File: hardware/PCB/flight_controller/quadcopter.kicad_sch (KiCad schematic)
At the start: 31 parts

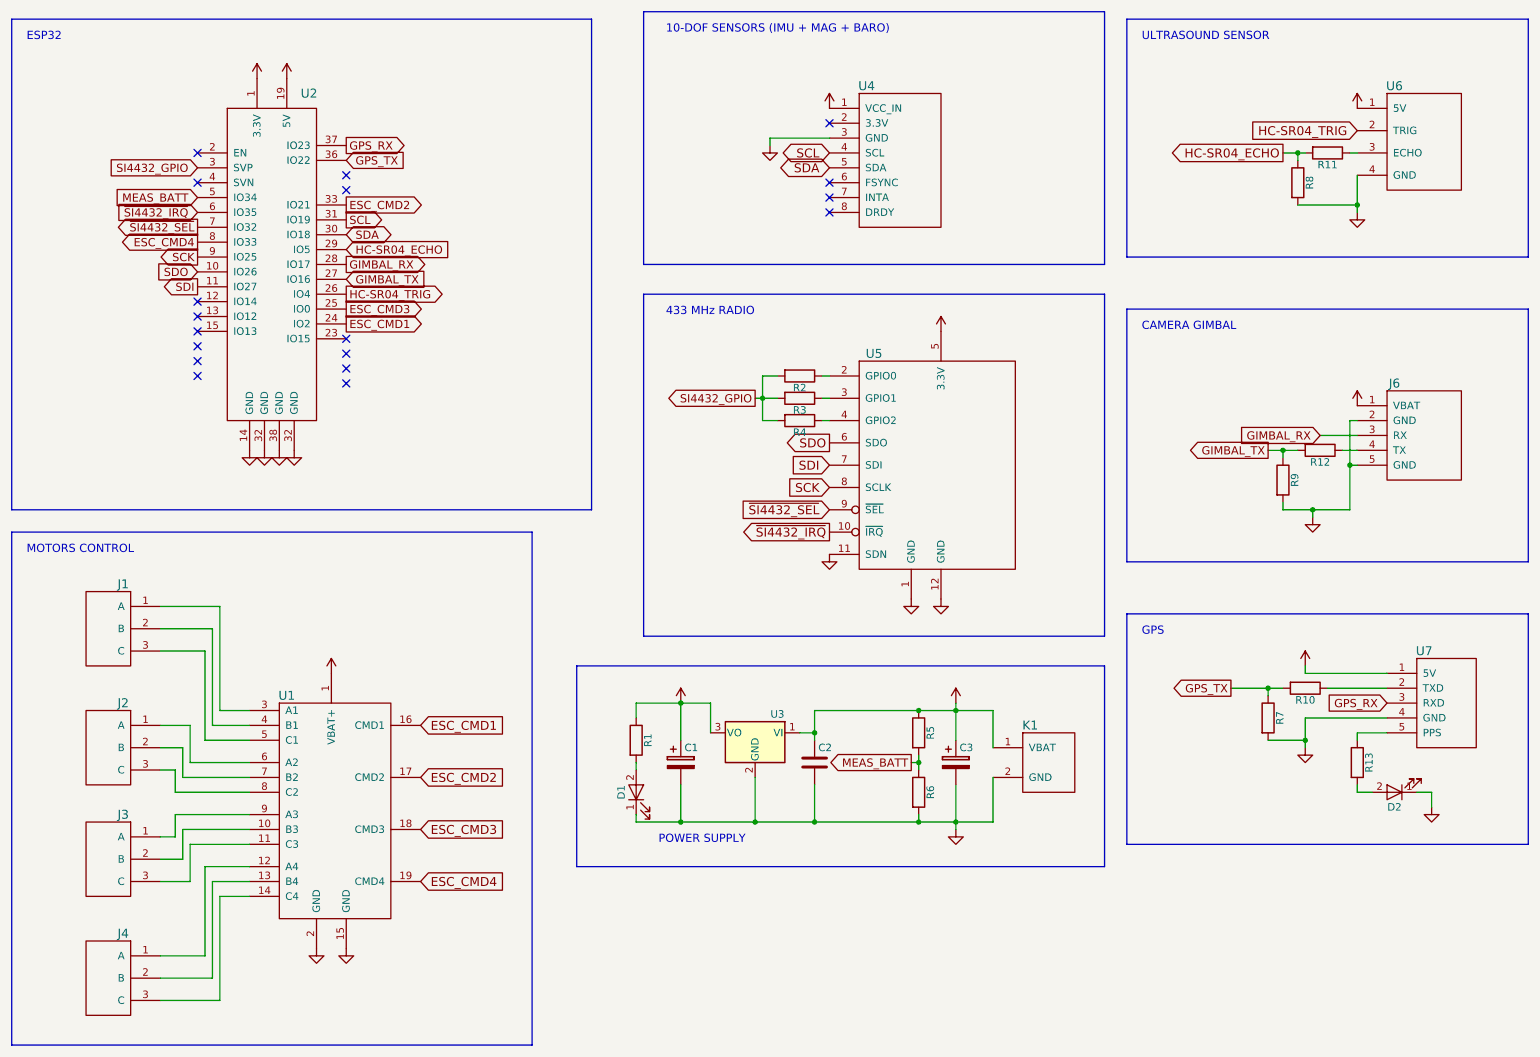
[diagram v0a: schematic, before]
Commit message: Move flight_controller PCB
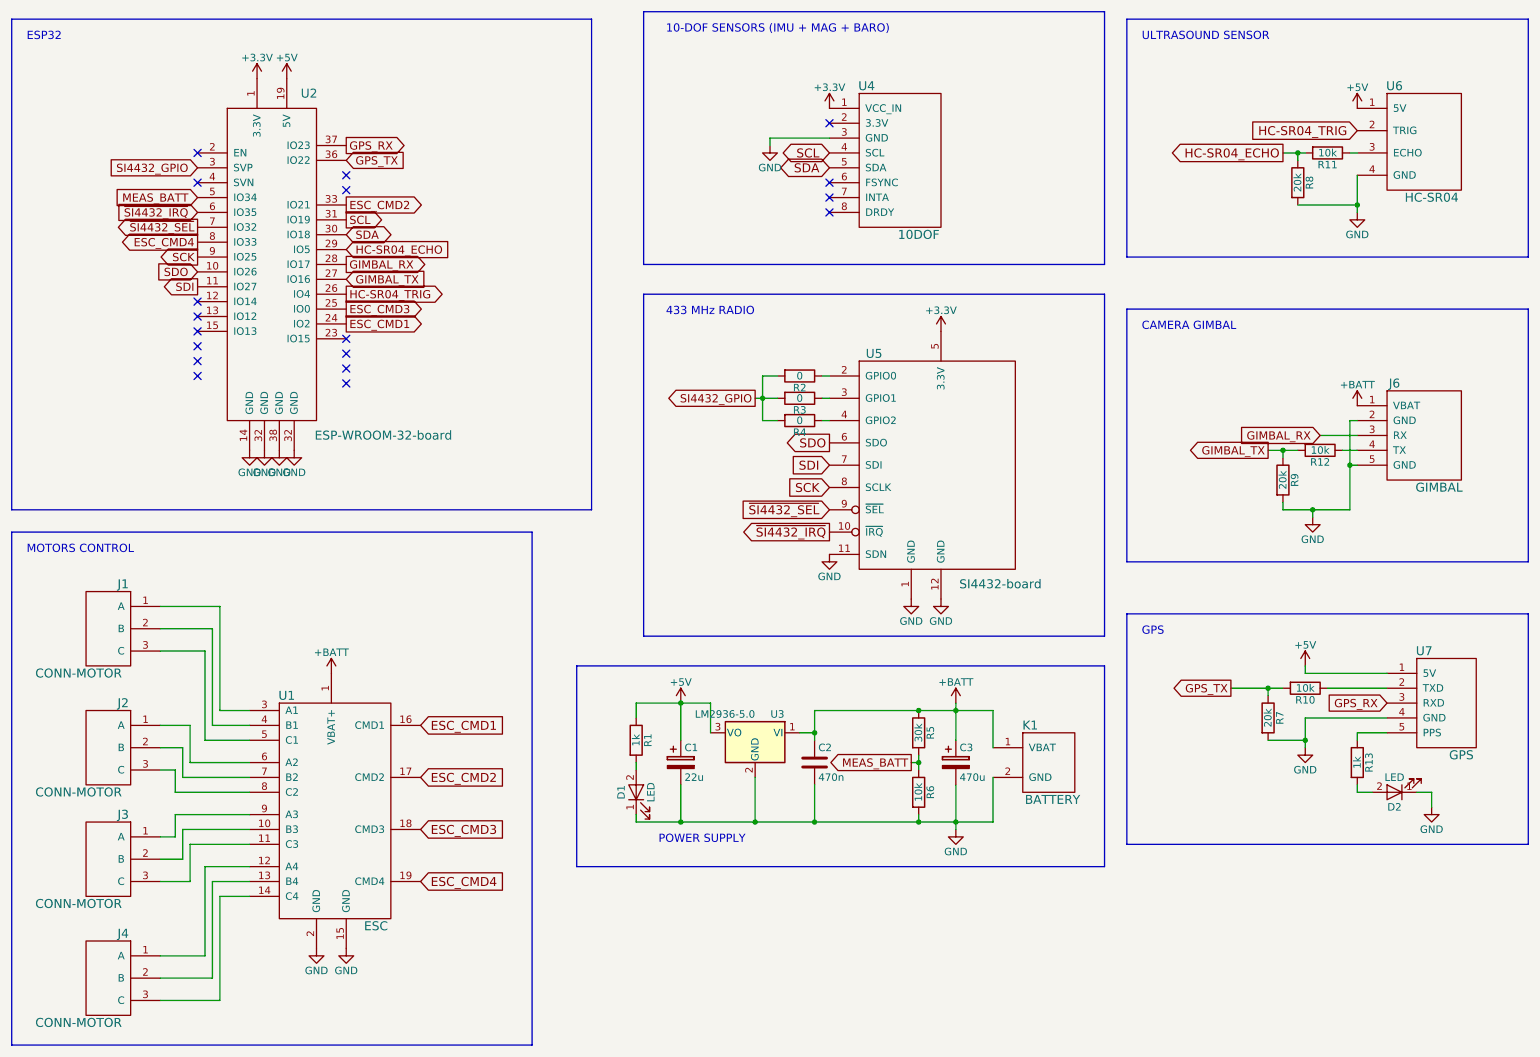
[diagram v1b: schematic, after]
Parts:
- C1: value (none) -> 22u; footprint (none) -> Capacitor_THT:CP_Radial_D5.0mm_P2.50mm
- C2: value (none) -> 470n; footprint (none) -> Capacitor_SMD:C_1206_3216Metric_Pad1.42x1.75mm_HandSolder
- C3: value (none) -> 470u; footprint (none) -> Capacitor_THT:CP_Radial_D10.0mm_P5.00mm
- D1, D2: value (none) -> LED; footprint (none) -> LED_SMD:LED_1206_3216Metric_Pad1.42x1.75mm_HandSolder
- J1, J2, J3, J4: value (none) -> CONN-MOTOR; footprint (none) -> quadcopter:motor-connector
- J6: value (none) -> GIMBAL; footprint (none) -> quadcopter:GIMBAL
- K1: value (none) -> BATTERY; footprint (none) -> quadcopter:battery-connector
- R1, R13: value (none) -> 1k; footprint (none) -> Resistor_SMD:R_1206_3216Metric_Pad1.42x1.75mm_HandSolder
- R10, R11, R12, R6: value (none) -> 10k; footprint (none) -> Resistor_SMD:R_1206_3216Metric_Pad1.42x1.75mm_HandSolder
- R2, R3, R4: value (none) -> 0; footprint (none) -> Resistor_SMD:R_1206_3216Metric_Pad1.42x1.75mm_HandSolder
- R5: value (none) -> 30k; footprint (none) -> Resistor_SMD:R_1206_3216Metric_Pad1.42x1.75mm_HandSolder
- R7, R8, R9: value (none) -> 20k; footprint (none) -> Resistor_SMD:R_1206_3216Metric_Pad1.42x1.75mm_HandSolder
- U1: value (none) -> ESC; footprint (none) -> quadcopter:ESC
- U2: value (none) -> ESP-WROOM-32-board; footprint (none) -> quadcopter:ESP32-VROOM-board
- U3: value (none) -> LM2936-5.0; footprint (none) -> Package_TO_SOT_SMD:TO-263-2
- U4: value (none) -> 10DOF; footprint (none) -> quadcopter:10DOF
- U5: value (none) -> SI4432-board; footprint (none) -> quadcopter:SI4432-board
- U6: value (none) -> HC-SR04; footprint (none) -> quadcopter:HC-SR04
- U7: value (none) -> GPS; footprint (none) -> quadcopter:GPS
